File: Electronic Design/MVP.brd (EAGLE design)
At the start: 88.6 x 68 mm, 35 parts, among them IC1 ACS712ELC-5A, IC2 ATMEGA328-PU, Q1 IRF9540, Q2 IRF9540, X1 16MHz

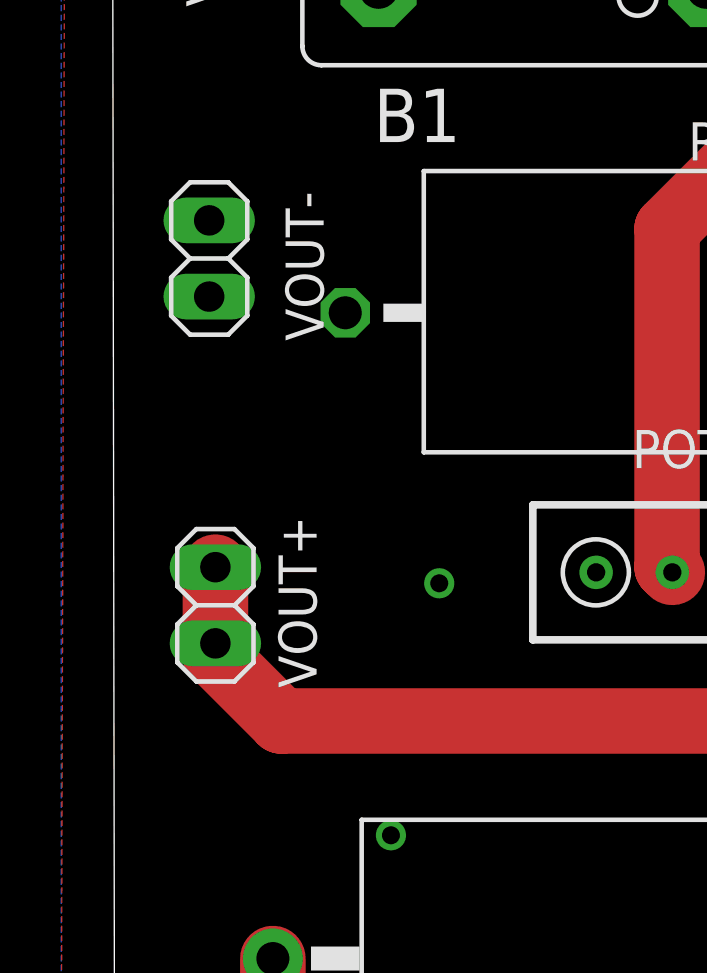
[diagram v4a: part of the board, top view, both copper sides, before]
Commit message: moved VIN+ and VIN- to allow more space between components
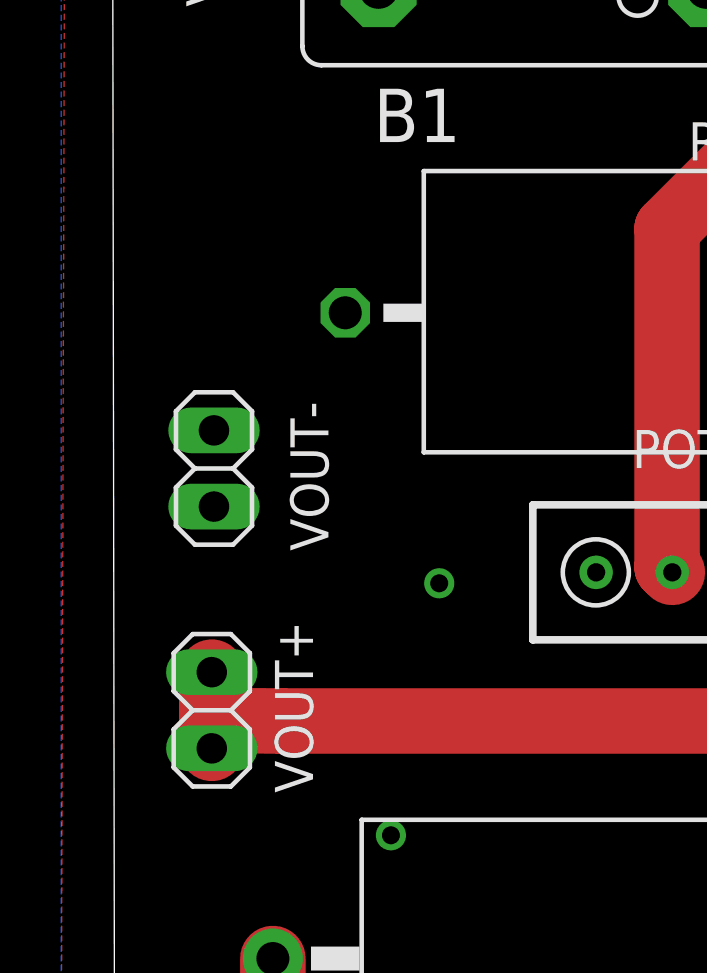
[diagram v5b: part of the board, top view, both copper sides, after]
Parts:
- moved VOUT- 7.00 mm to (3.50, 34.2)
- moved VOUT+ 3.50 mm to (3.42, 26.1)
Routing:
- net M1S: track 48.9 -> 47.7 mm
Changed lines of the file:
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@@
 <attribute name="VALUE" x="-0.430584375" y="59.729996875" size="1.27" layer="27" rot="R270"/>
 </element>
-<element name="VOUT+" library="pinhead" package="1X02" value="" x="3.544190625" y="29.647540625" smashed="yes" rot="R270">
-<attribute name="NAME" x="6.918396875" y="26.896659375" size="1.27" layer="25" ratio="10" rot="R90"/>
-<attribute name="VALUE" x="0.369190625" y="32.187540625" size="1.27" layer="27" rot="R270"/>
+<element name="VOUT+" library="pinhead" package="1X02" value="" x="3.424190625" y="26.147540625" smashed="yes" rot="R270">
+<attribute name="NAME" x="6.798396875" y="23.396659375" size="1.27" layer="25" ratio="10" rot="R90"/>
+<attribute name="VALUE" x="0.249190625" y="28.687540625" size="1.27" layer="27" rot="R270"/>
 </element>
 <element name="F1" library="fuse" package="FUSE_HOLDER_5X20MM" value="FUSEBLANK_5X20MM" x="26.974415625" y="60.299996875" smashed="yes">
@@
 <element name="C8" library="resistor" package="C0805K" value="22n" x="74.379803125" y="47.5407875" rot="R270"/>
 <element name="JP2" library="pinhead" package="1X08" value="" x="56.8750375" y="51.21298125" rot="R270"/>
-<element name="VOUT-" library="pinhead" package="1X02" value="" x="3.33730625" y="41.2068625" smashed="yes" rot="R90">
-<attribute name="NAME" x="5.88288125" y="43.4397375" size="1.27" layer="25" ratio="10" rot="R270"/>
-<attribute name="VALUE" x="6.51230625" y="37.3968625" size="1.27" layer="27" rot="R90"/>
+<element name="VOUT-" library="pinhead" package="1X02" value="" x="3.49730625" y="34.2068625" smashed="yes" rot="R90">
+<attribute name="NAME" x="6.04288125" y="36.4397375" size="1.27" layer="25" ratio="10" rot="R270"/>
+<attribute name="VALUE" x="6.67230625" y="30.3968625" size="1.27" layer="27" rot="R90"/>
 </element>
 <element name="VIN_BUCK" library="pinhead" package="1X02" value="" x="85.50119375" y="29.554190625" rot="R90"/>
@@
 <contactref element="IC1" pad="4"/>
 <contactref element="VOUT+" pad="2"/>
-<wire x1="3.544190625" y1="28.377540625" x2="3.544190625" y2="30.917540625" width="2.1844" layer="1"/>
+<wire x1="3.424190625" y1="25.805809375" x2="3.424190625" y2="27.417540625" width="2.1844" layer="1"/>
 <wire x1="40.08365625" y1="36.6083875" x2="40.5916125" y2="36.6083875" width="2.1844" layer="1"/>
 <wire x1="40.5916125" y1="36.6083875" x2="40.6" y2="36.6" width="2.1844" layer="1"/>
@@
 <wire x1="33.14" y1="26.81" x2="30.9159875" y2="26.81" width="2.1844" layer="1"/>
 <wire x1="30.9159875" y1="26.81" x2="30.902703125" y2="26.823284375" width="2.1844" layer="1"/>
-<wire x1="3.544190625" y1="28.377540625" x2="3.544190625" y2="27.985809375" width="2.1844" layer="1"/>
-<wire x1="3.544190625" y1="27.985809375" x2="5.74" y2="25.79" width="2.1844" layer="1"/>
+<wire x1="3.424190625" y1="24.877540625" x2="3.424190625" y2="25.805809375" width="2.1844" layer="1"/>
+<wire x1="3.424190625" y1="25.805809375" x2="5.74" y2="25.79" width="2.1844" layer="1"/>
 <wire x1="5.74" y1="25.79" x2="29.86941875" y2="25.79" width="2.1844" layer="1"/>
 <wire x1="29.86941875" y1="25.79" x2="30.902703125" y2="26.823284375" width="2.1844" layer="1"/>
